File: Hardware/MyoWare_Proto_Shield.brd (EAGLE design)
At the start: 52.1 x 20.8 mm, 27 parts

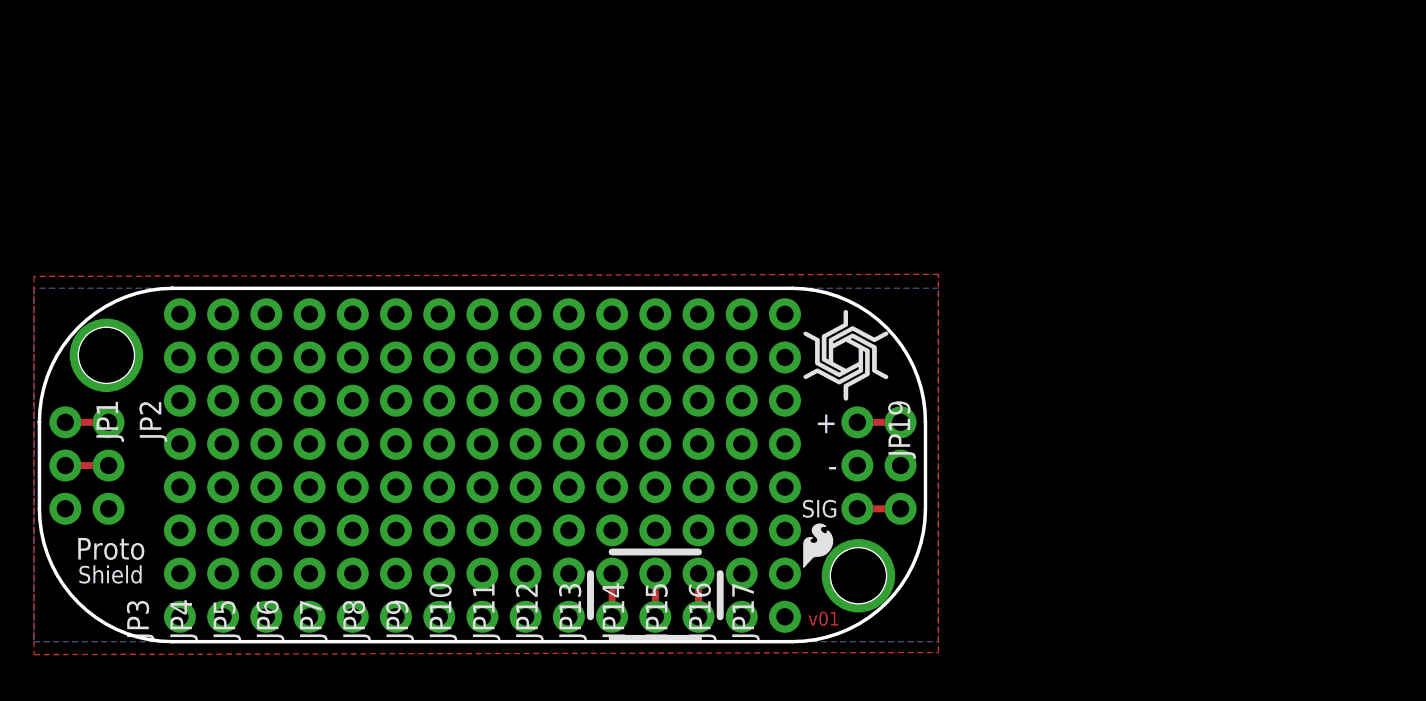
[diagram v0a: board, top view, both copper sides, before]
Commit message: Tweaks to meet SFE checklist
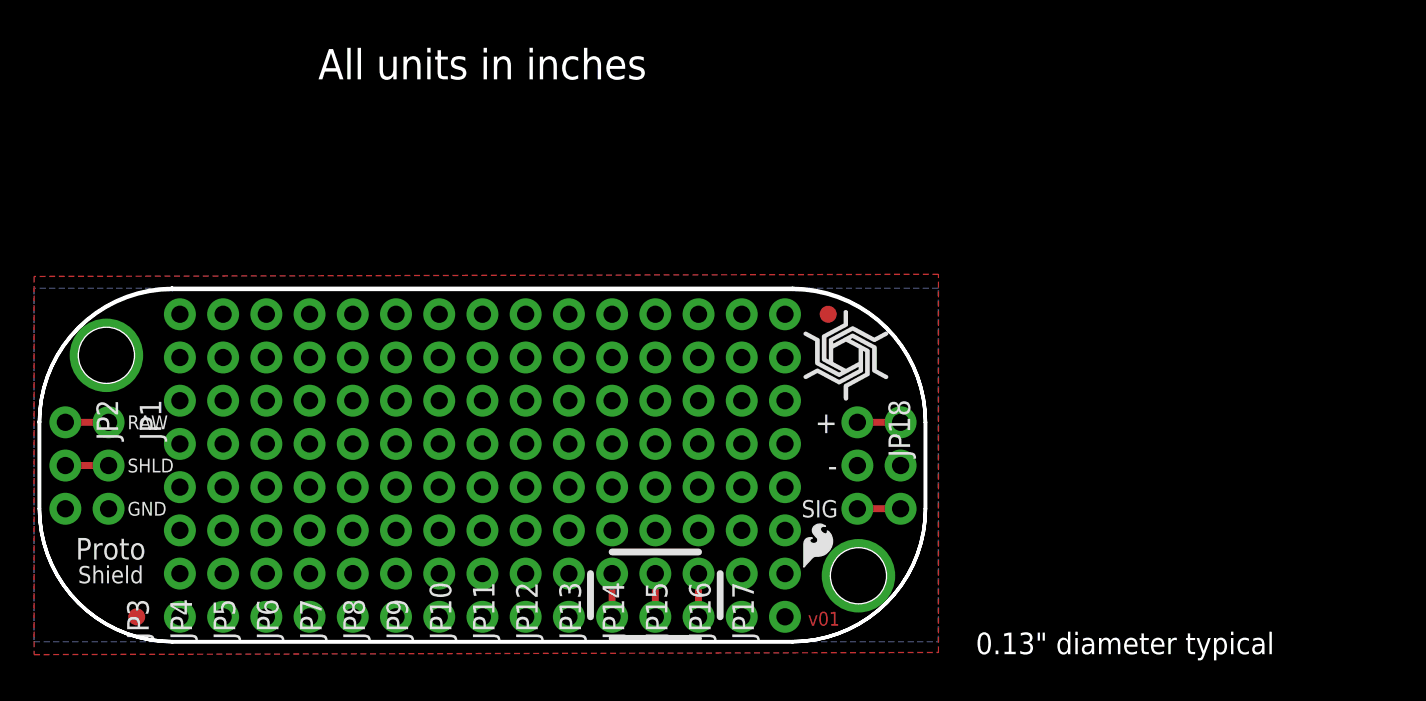
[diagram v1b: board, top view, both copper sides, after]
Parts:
- added FID1, FID2: FIDUCIAL1X2, SparkFun-Aesthetics:FIDUCIAL-1X2
- moved JP1 2.54 mm to (-22.0, 2.54)
- moved JP18 2.54 mm to (22.0, 2.54)
- moved JP19 2.54 mm to (24.6, 2.54)
- moved JP2 2.54 mm to (-24.5, 2.54)
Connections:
- net +VS renamed VCC
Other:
- outline, holes or cut-outs redrawn
- board text added: "0.13" diameter typical"
- board text added: "All units in inches"
- board text added: "GND"
- board text added: "RAW"
- board text added: "SHLD"

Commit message: Copied remote silk to bottom
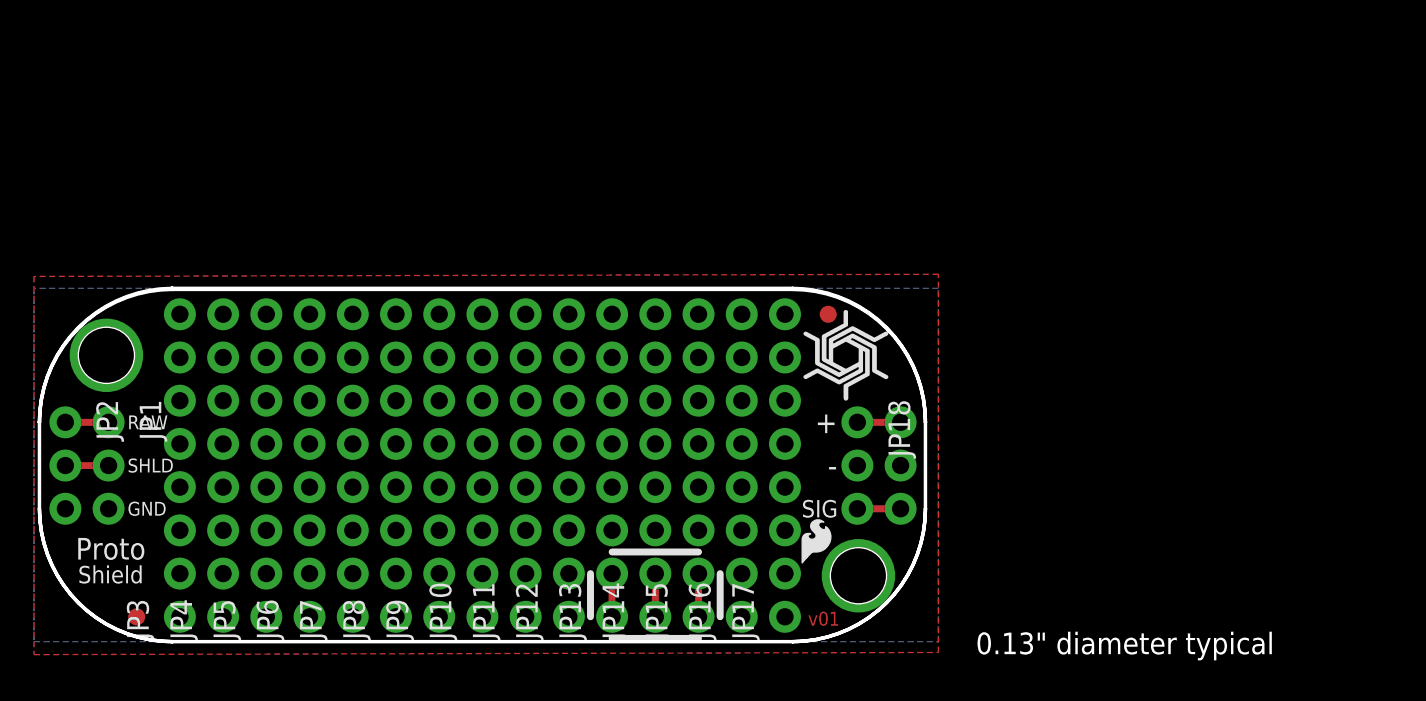
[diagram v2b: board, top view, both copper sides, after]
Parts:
- moved LOGO1 0.27 mm to (18.5, -6.08)

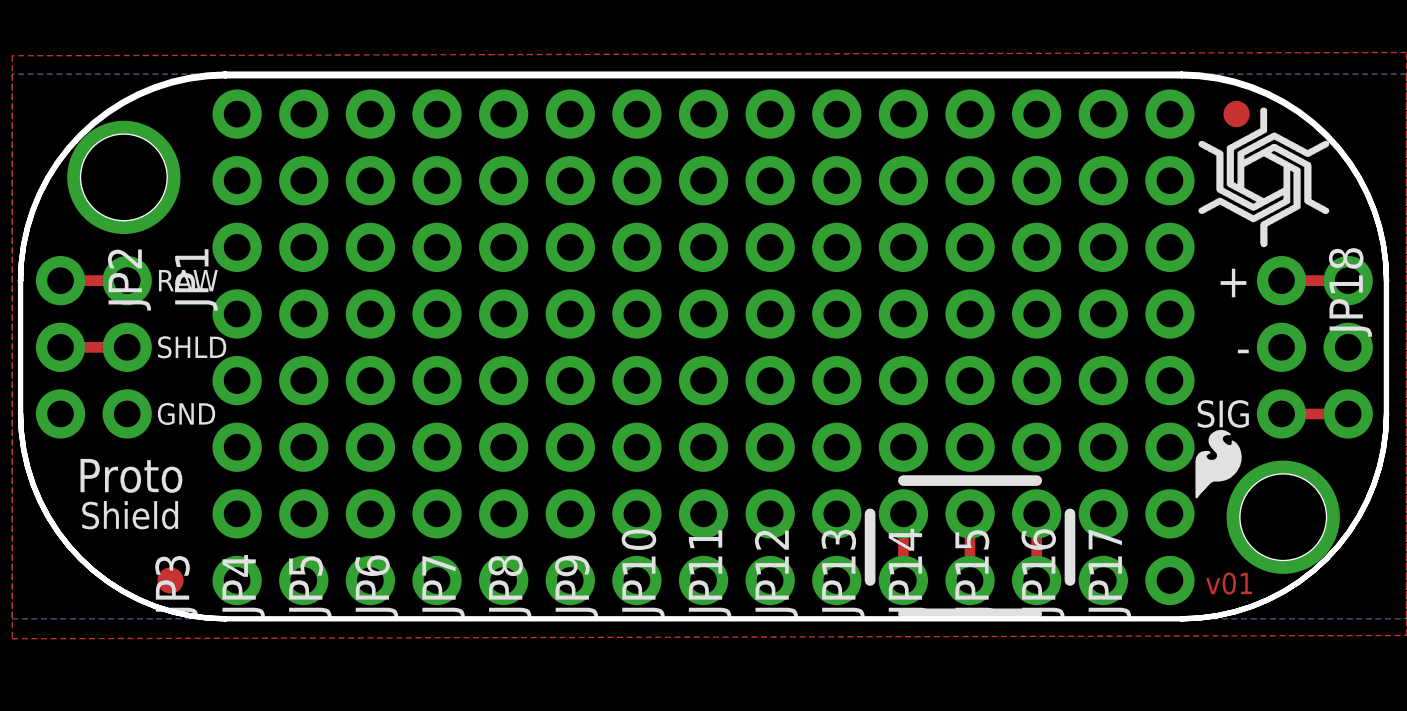
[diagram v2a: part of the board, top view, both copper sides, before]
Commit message: Removed fiducials
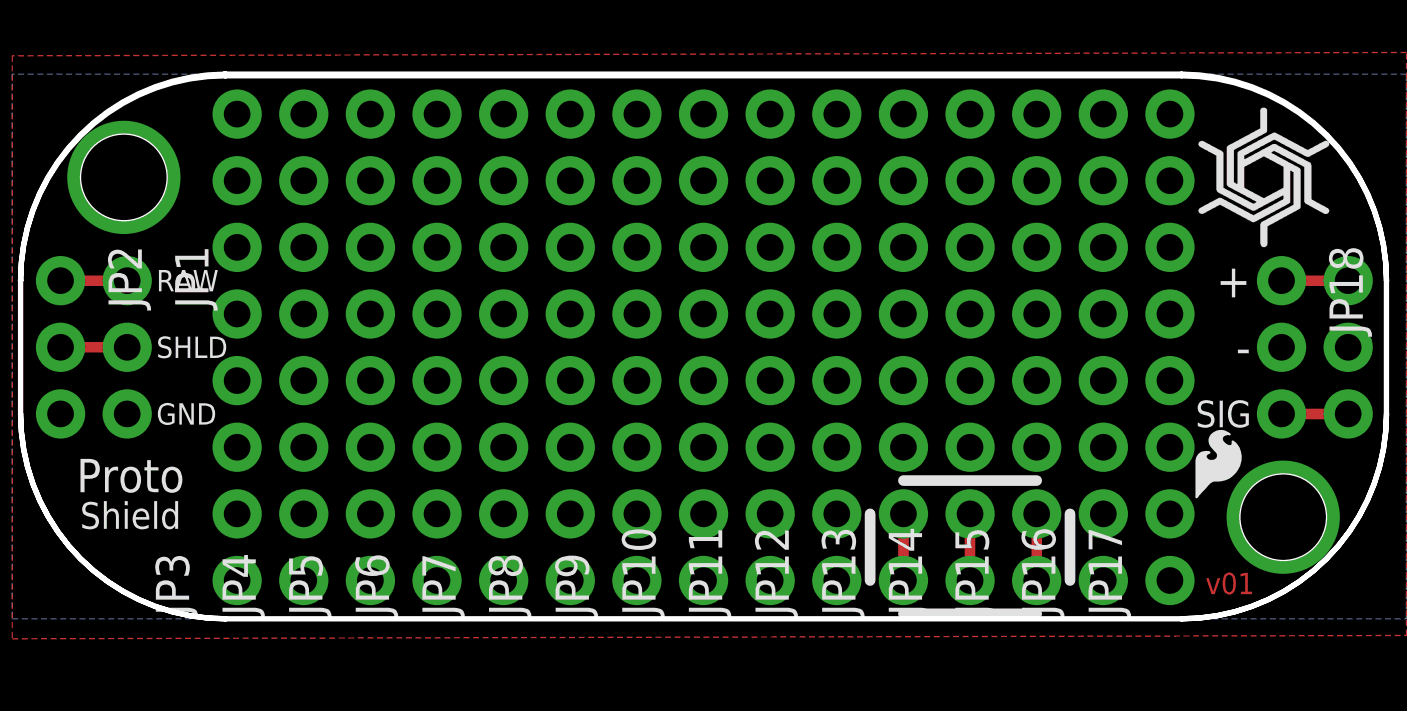
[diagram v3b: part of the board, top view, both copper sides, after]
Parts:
- removed FID1, FID2: FIDUCIAL1X2, SparkFun-Aesthetics:FIDUCIAL-1X2
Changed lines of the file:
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@@
 <element name="LOGO1" library="SparkFun-Aesthetics" package="SFE_LOGO_FLAME_.1" value="SFE_LOGO_FLAME.1_INCH" x="18.47" y="-6.08"/>
 <element name="LOGO2" library="SparkFun-Aesthetics" package="OSHW-LOGO-S" value="OSHW-LOGOS" x="21.59" y="6.35" rot="MR0"/>
-<element name="FID1" library="SparkFun-Aesthetics" package="FIDUCIAL-1X2" value="FIDUCIAL1X2" x="20.32" y="8.89"/>
-<element name="FID2" library="SparkFun-Aesthetics" package="FIDUCIAL-1X2" value="FIDUCIAL1X2" x="-20.32" y="-8.89"/>
 </elements>
 <signals>

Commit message: Updated version to 10
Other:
- board text added: "v10"
- board text removed: "v01"
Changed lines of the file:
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@@
 <?xml version="1.0" encoding="utf-8"?>
 <!DOCTYPE eagle SYSTEM "eagle.dtd">
-<eagle version="7.3.1">
+<eagle version="7.3.2">
 <drawing>
 <settings>
@@
 <wire x1="13.97" y1="-6.35" x2="13.97" y2="-8.89" width="0.4064" layer="21"/>
 <wire x1="12.7" y1="-10.16" x2="7.62" y2="-10.16" width="0.4064" layer="21"/>
-<text x="19.13" y="-9.41" size="0.8128" layer="1" font="vector" ratio="20">v01</text>
+<text x="19.13" y="-9.41" size="0.8128" layer="1" font="vector" ratio="20">v10</text>
 <text x="-2.54" y="-20.32" size="1.778" layer="51" font="vector">Brian E Kaminski of Advancer Technologies</text>
 <text x="-21.59" y="-22.86" size="1.778" layer="51" font="vector">Revised by: Brent Wilkins</text>
